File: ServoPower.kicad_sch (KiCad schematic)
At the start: 0 parts

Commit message: Fixed Merge Conflicts
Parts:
- added C1: 100uF, symbol Device:C_Small_US
- added C2: 470uF, symbol Device:C_Small_US
- added Cfeedback1: 1nF, symbol Device:C_Small
- added D1: 550mV, symbol Device:D_Schottky
- added L1: 82uH, symbol Device:L
- added Rfeedback1: 1k, symbol Device:R_Small_US
- added Rfeedback2: 3.83k, symbol Device:R_Small_US
- added U1: LM2596T-ADJ/LF02, NEB5_TEX, symbol 2026-01-27_05-04-46:LM2596T-ADJ_LF02
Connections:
- new net: Cfeedback1.1, Rfeedback1.1, Rfeedback2.1, U1.4 (FEEDBACK)
- new net: D1.1 (K), L1.1, U1.2 (OUTPUT)
- new net +12V: C1.1, U1.1 (VIN)
- new net GND: C1.2, C2.1, C2.2, Cfeedback1.2, D1.2 (A), L1.2, Rfeedback1.2, Rfeedback2.2, U1.3 (GROUND)

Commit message: Revert "Fixed Merge Conflicts"
This reverts commit 1dcac9fe20d43ad9866d81964f948f071540213e.
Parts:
- removed C1: 100uF, symbol Device:C_Small_US
- removed C2: 470uF, symbol Device:C_Small_US
- removed Cfeedback1: 1nF, symbol Device:C_Small
- removed D1: 550mV, symbol Device:D_Schottky
- removed L1: 82uH, symbol Device:L
- removed Rfeedback1: 1k, symbol Device:R_Small_US
- removed Rfeedback2: 3.83k, symbol Device:R_Small_US
- removed U1: LM2596T-ADJ/LF02, NEB5_TEX, symbol 2026-01-27_05-04-46:LM2596T-ADJ_LF02

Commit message: Servo Power added to child
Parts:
- added C1: 100uF, symbol Device:C_Small_US
- added C2: 470uF, symbol Device:C_Small_US
- added Cfeedback1: 1nF, symbol Device:C_Small
- added D1: 550mV, symbol Device:D_Schottky
- added L1: 82uH, symbol Device:L
- added Rfeedback1: 1k, symbol Device:R_Small_US
- added Rfeedback2: 3.83k, symbol Device:R_Small_US
- added U1: LM2596T-ADJ/LF02, NEB5_TEX, symbol 2026-01-27_05-04-46:LM2596T-ADJ_LF02
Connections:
- new net: Cfeedback1.1, Rfeedback1.1, Rfeedback2.1, U1.4 (FEEDBACK)
- new net: D1.1 (K), L1.1, U1.2 (OUTPUT)
- new net +12V: C1.1, U1.1 (VIN)
- new net GND: C1.2, C2.1, C2.2, Cfeedback1.2, D1.2 (A), L1.2, Rfeedback1.2, Rfeedback2.2, U1.3 (GROUND)

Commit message: Added footprints
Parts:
- C1: footprint (none) -> Capacitor_SMD:C_Elec_6.3x5.4
- C2: footprint (none) -> Capacitor_SMD:C_Elec_10x10.2
- Cfeedback1: footprint (none) -> Capacitor_SMD:C_0603_1608Metric
- D1: footprint (none) -> Diode_SMD:D_3220_8050Metric
- L1: footprint (none) -> Inductor_SMD:L_Bourns_SRR1260
- Rfeedback1, Rfeedback2: footprint (none) -> Resistor_SMD:R_0805_2012Metric
- U1: footprint NEB5_TEX -> (none)
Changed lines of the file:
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@@
 			)
 		)
-		(property "Footprint" ""
+		(property "Footprint" "Capacitor_SMD:C_0603_1608Metric"
 			(at 198.12 52.07 0)
 			(effects
@@
 			)
 		)
-		(property "Footprint" ""
+		(property "Footprint" "Capacitor_SMD:C_Elec_6.3x5.4"
 			(at 104.14 102.87 0)
 			(effects
@@
 			)
 		)
-		(property "Footprint" ""
+		(property "Footprint" "Inductor_SMD:L_Bourns_SRR1260"
 			(at 204.47 82.55 0)
 			(effects
@@
 			)
 		)
-		(property "Footprint" ""
+		(property "Footprint" "Resistor_SMD:R_0805_2012Metric"
 			(at 184.15 52.07 0)
 			(effects
@@
 			)
 		)
-		(property "Footprint" "NEB5_TEX"
+		(property "Footprint" ""
 			(at 113.03 83.82 0)
 			(effects
@@
 			)
 		)
-		(property "Footprint" ""
+		(property "Footprint" "Resistor_SMD:R_0805_2012Metric"
 			(at 198.12 64.77 0)
 			(effects
@@
 			)
 		)
-		(property "Footprint" ""
+		(property "Footprint" "Capacitor_SMD:C_Elec_10x10.2"
 			(at 214.63 100.33 0)
 			(effects
@@
 			)
 		)
-		(property "Footprint" ""
+		(property "Footprint" "Diode_SMD:D_3220_8050Metric"
 			(at 184.15 101.6 0)
 			(effects

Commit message: ICs added
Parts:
- U1: footprint (none) -> LM2596T-ADJ_LF02:TO170P470X1016X2092-5P
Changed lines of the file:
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@@
 			)
 		)
-		(property "Footprint" ""
+		(property "Footprint" "LM2596T-ADJ_LF02:TO170P470X1016X2092-5P"
 			(at 113.03 83.82 0)
 			(effects

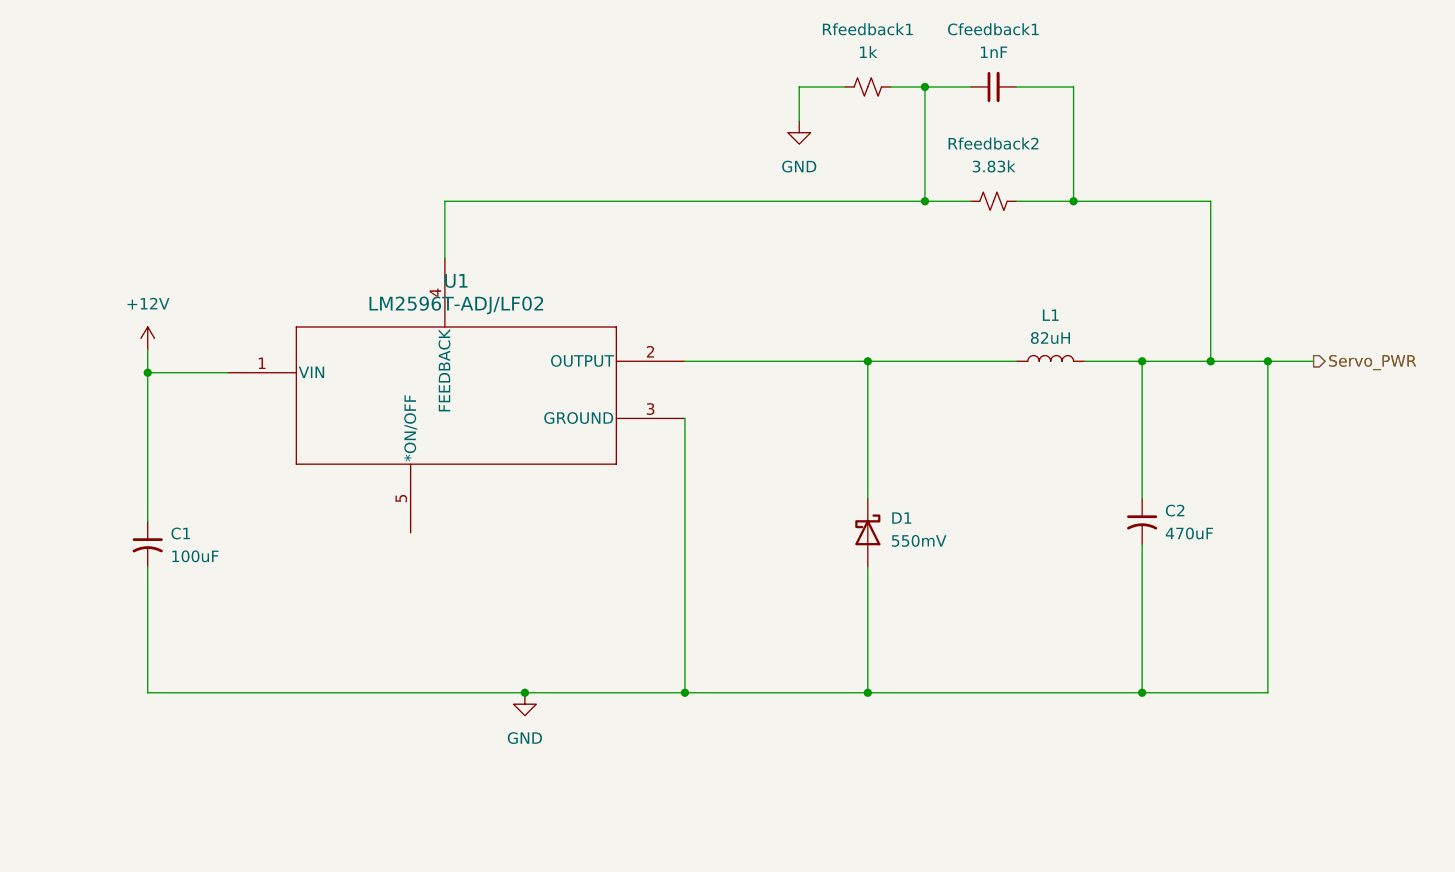
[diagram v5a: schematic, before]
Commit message: PCB Placement and Planes
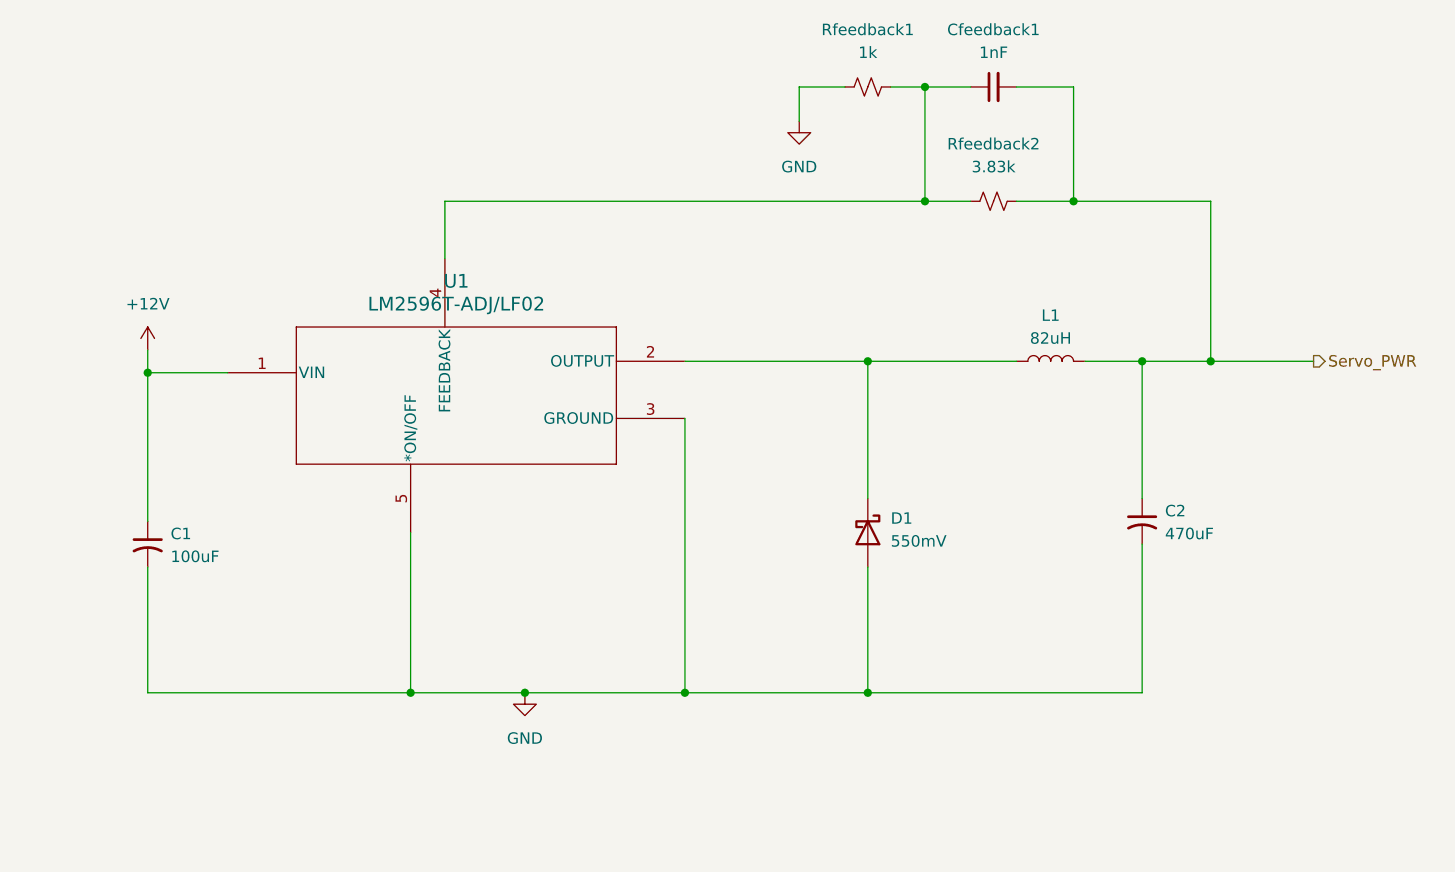
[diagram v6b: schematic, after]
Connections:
- net GND: now also U1.5 (*ON/OFF); no longer C2.1, Cfeedback1.2, L1.2, Rfeedback2.2
- new net Servo_PWR: C2.1, Cfeedback1.2, L1.2, Rfeedback2.2
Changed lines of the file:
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@@
-	)
-	(junction
-		(at 228.6 82.55)
-		(diameter 0)
-		(color 0 0 0 0)
 	)
 	(junction
@@
 	)
 	(junction
-		(at 214.63 119.38)
+		(at 133.35 119.38)
 		(diameter 0)
 		(color 0 0 0 0)
@@
 	(wire
 		(pts
-			(xy 104.14 119.38) (xy 146.05 119.38)
+			(xy 104.14 119.38) (xy 133.35 119.38)
 		)
 		(stroke
@@
 	(wire
 		(pts
-			(xy 214.63 119.38) (xy 228.6 119.38)
-		)
-		(stroke
-			(width 0)
-			(type default)
-		)
-	)
-	(wire
-		(pts
 			(xy 207.01 52.07) (xy 207.01 64.77)
 		)
@@
 	(wire
 		(pts
-			(xy 228.6 82.55) (xy 233.68 82.55)
+			(xy 222.25 82.55) (xy 233.68 82.55)
 		)
 		(stroke
@@
 	(wire
 		(pts
+			(xy 133.35 119.38) (xy 146.05 119.38)
+		)
+		(stroke
+			(width 0)
+			(type default)
+		)
+	)
+	(wire
+		(pts
 			(xy 186.69 52.07) (xy 190.5 52.07)
 		)
@@
 	(wire
 		(pts
-			(xy 228.6 82.55) (xy 228.6 119.38)
-		)
-		(stroke
-			(width 0)
-			(type default)
-		)
-	)
-	(wire
-		(pts
-			(xy 222.25 82.55) (xy 228.6 82.55)
-		)
-		(stroke
-			(width 0)
-			(type default)
-		)
-	)
-	(wire
-		(pts
 			(xy 214.63 82.55) (xy 222.25 82.55)
 		)
@@
 		)
 		(stroke
+			(width 0)
+			(type default)
+		)
+	)
+	(wire
+		(pts
+			(xy 133.35 101.6) (xy 133.35 119.38)
+		)
+		(stroke

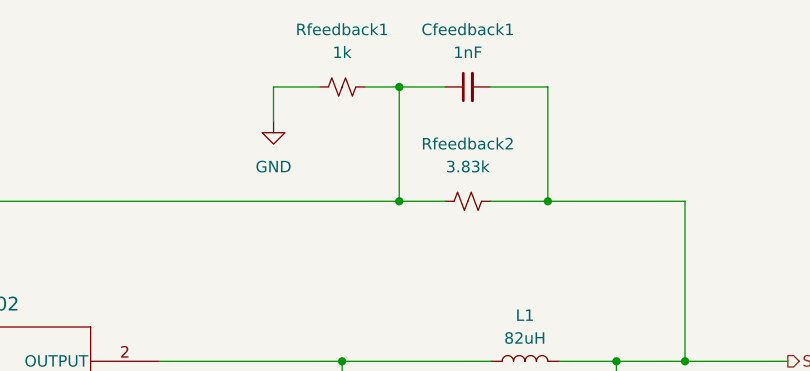
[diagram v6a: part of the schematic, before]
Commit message: Fixed DRC errors
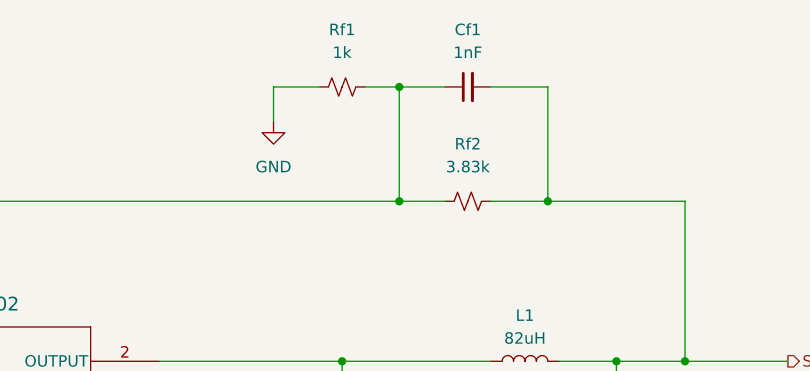
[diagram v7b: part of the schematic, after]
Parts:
- renumbered Cfeedback1 to Cf1, Rfeedback1 to Rf1, Rfeedback2 to Rf2
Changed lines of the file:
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@@
 		(dnp no)
 		(fields_autoplaced yes)
-		(property "Reference" "Cfeedback1"
+		(property "Reference" "Cf1"
 			(at 198.1263 45.72 90)
 			(effects
@@
 			(project "PAFT_pcbs"
 				(path "/8372e765-ead7-42d0-82da-59a3937ad504/15a8a804-fdd6-4fa4-9fe0-6b70c3520bb0"
-					(reference "Cfeedback1")
+					(reference "Cf1")
 					(unit 1)
 				)
@@
 		(dnp no)
 		(fields_autoplaced yes)
-		(property "Reference" "Rfeedback1"
+		(property "Reference" "Rf1"
 			(at 184.15 45.72 90)
 			(effects
@@
 			(project "PAFT_pcbs"
 				(path "/8372e765-ead7-42d0-82da-59a3937ad504/15a8a804-fdd6-4fa4-9fe0-6b70c3520bb0"
-					(reference "Rfeedback1")
+					(reference "Rf1")
 					(unit 1)
 				)
@@
 		(dnp no)
 		(fields_autoplaced yes)
-		(property "Reference" "Rfeedback2"
+		(property "Reference" "Rf2"
 			(at 198.12 58.42 90)
 			(effects
@@
 			(project "PAFT_pcbs"
 				(path "/8372e765-ead7-42d0-82da-59a3937ad504/15a8a804-fdd6-4fa4-9fe0-6b70c3520bb0"
-					(reference "Rfeedback2")
-					(unit 1)
-				)
+					(reference "Rf2")
+					(unit 1)
+				)
